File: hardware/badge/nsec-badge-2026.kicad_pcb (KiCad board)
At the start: 4 copper layers, 159.8 x 139.1 mm, 180 parts, among them J1001 Conn_01x01_Female, J1002 Conn_01x01_Female, J1003 Conn_01x01_Female, J1004 Conn_01x01_Female, J1005 Conn_01x01_Female, J1006 Conn_01x01_Female, J1007 Conn_01x01_Female, J1008 Conn_01x01_Female, J701 PM254-2-03-S-8_5, J702 PM254-2-03-S-8_5, J901 Bus_PCI_32bit_Universal, P1001 U.FL-R-SMT-1_10_, P1002 U.FL-R-SMT-1_10_, Q1201 IRLML0100TRPBF, SW201 TS-1187A-C-C-B, SW202 TS-1187A-C-C-B, SW601 TS-1187A-C-C-B, SW602 TS-1187A-C-C-B, SW603 TS-1187A-C-C-B, SW604 TS-1187A-C-C-B, SW605 TS-1187A-C-C-B, SW606 TS-1187A-C-C-B, U1001 ST25R3916-AQWT, U1101 VEML6040A3OG, U1202 HC-FPC-05-09-24RLTAG, U201 ESP32-S3-WROOM-1(N16R8), U301 AP2112K-3_3TRG1, U401 TYPE-C-31-M-12, U402 TPSMF05CT1G, U801 XT4054K421MR-G, U802 XDWF-0920-02P, Y1001 27.12Mhz

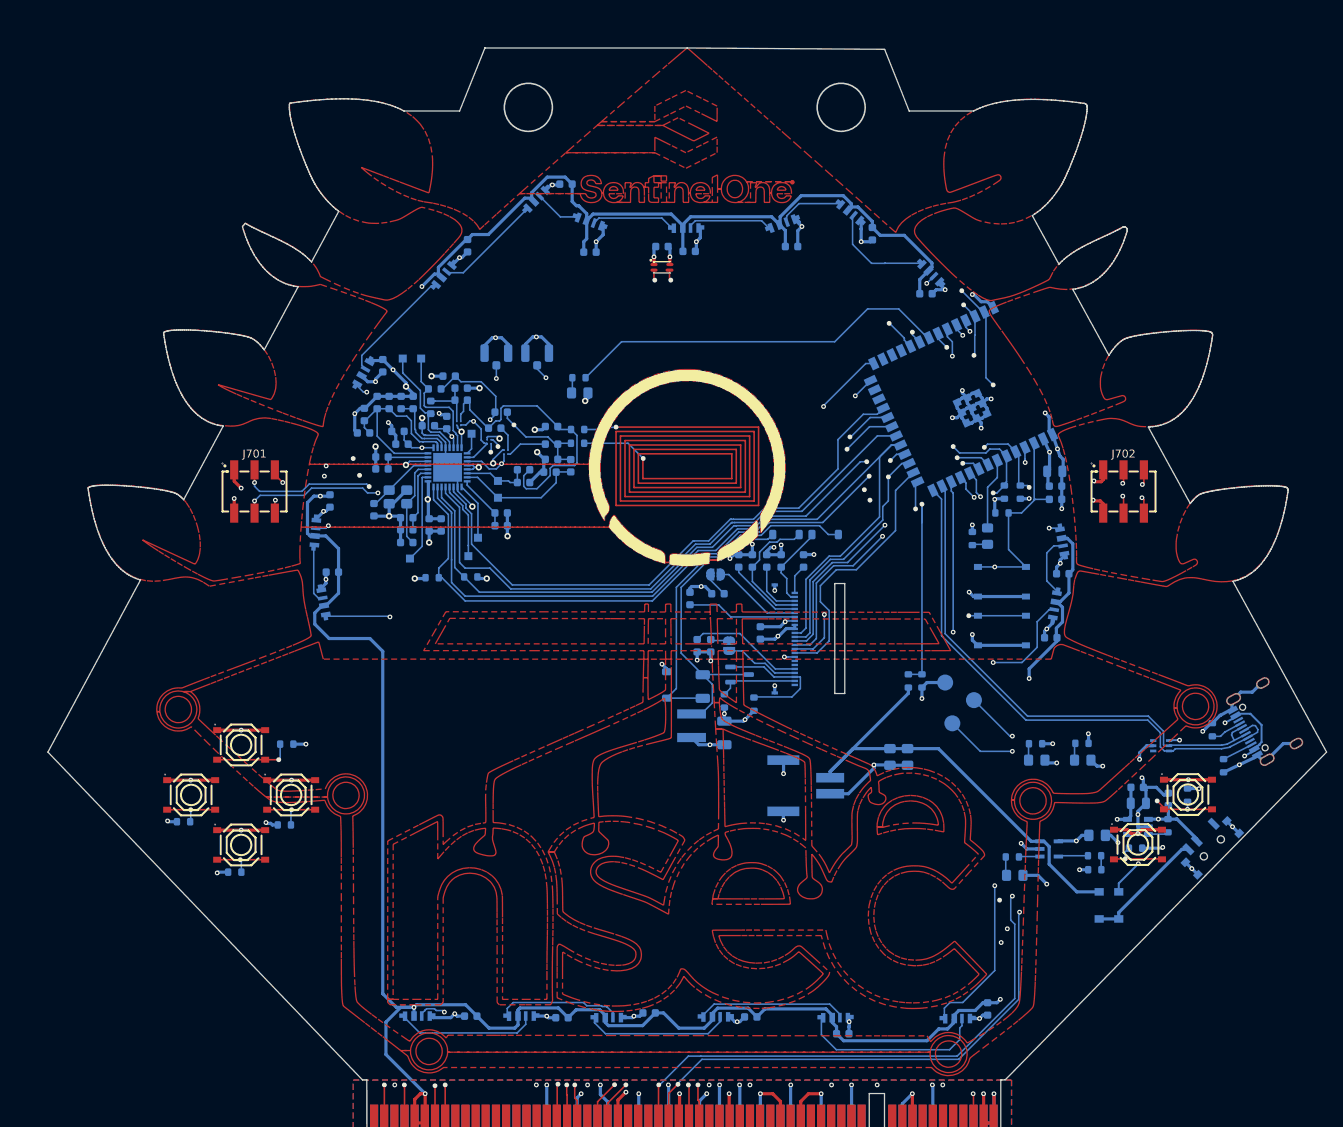
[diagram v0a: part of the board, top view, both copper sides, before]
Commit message: feat: badge v2 PCB design with panelization support
Updated schematic and PCB layout for badge v2 revision. Added
panelization project with JLCPCB production files, panelize script,
and board SVG artwork.
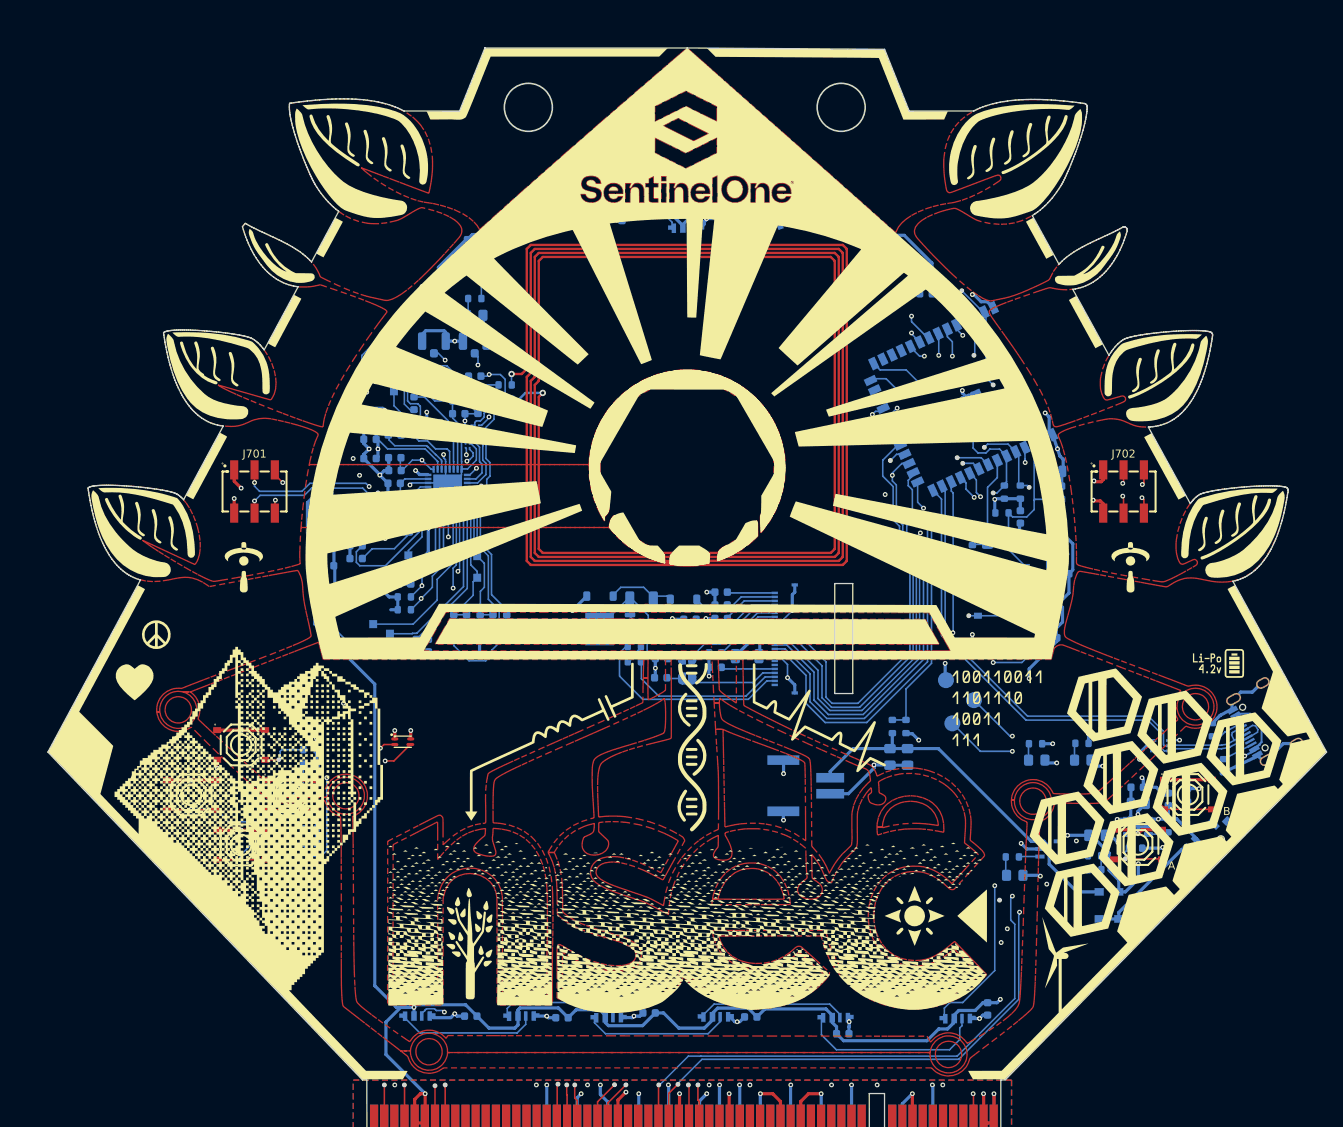
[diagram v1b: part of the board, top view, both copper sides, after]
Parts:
- removed the ? at (29.3, 30.1)
- added ? (x2): , Graphics, F.Cu at (29.4, 30.1)
- moved U1101 67.6 mm to (73.7, 116.8)
- moved C1101 56.1 mm to (150.9, 88.7), turned to -90 degrees
- moved C1030 27.9 mm to (84.1, 104.1)
- moved C1031 25.7 mm to (84.1, 105.9)
- moved C1035 24.3 mm to (80.1, 101.7), turned to -90 degrees
- moved C1029 22.8 mm to (86.7, 101.7), turned to -90 degrees
- moved C1034 21.3 mm to (81.7, 101.7), turned to 90 degrees
- moved D1203 19.5 mm to (108.8, 99.0), turned to 0 degrees
- moved C1032 19.3 mm to (85.0, 101.7), turned to 90 degrees
- moved C1006 18.9 mm to (76.9, 104.8), turned to -90 degrees
- moved C1004 18.3 mm to (75.4, 104.8), turned to -90 degrees
- moved D1201 18.2 mm to (108.8, 103.8)
- moved C1033 18.1 mm to (83.4, 101.7), turned to -90 degrees
- moved L1201 16.7 mm to (98.3, 102.7)
- moved R1001 16.4 mm to (82.7, 61.4)
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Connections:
- net Net-(R1004-Pad2) renamed /NFC/NFC_COIL
- C1011 pad 1: /NFC/VDD_TX -> +3V3
- C1012 pad 1: /NFC/VDD_TX -> +3V3
- C1015 pad 1: /NFC/VDD_TX -> +3V3
- C1016 pad 1: /NFC/VDD_TX -> +3V3
- C801 pad 1: VDD -> VBUS
- LED801 pad 2: VDD -> VBUS
- U1001 pad 10: /NFC/VDD_TX -> +3V3
- U1001 pad 8: /NFC/VDD_TX -> +3V3
- U801 pad 4: VDD -> VBUS
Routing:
- net /NFC/NFC_COIL: track 12.6 -> 616.7 mm
- net GND: track 395.7 -> 497.3 mm, vias 108 -> 103
- net /ESP32-S3/GPIO21: track 73.0 -> 123.2 mm, vias 0 -> 2
- net /ESP32-S3/GPIO12: track 74.0 -> 121.8 mm, vias 0 -> 2
- net Net-(C1026-Pt2): track 18.6 -> 65.0 mm, vias 2 -> 3
- net /SPI_MISO: track 79.7 -> 123.7 mm, vias 2 -> 3
- net Net-(D1202-A): track 42.8 -> 8.60 mm
- net +3V3: track 123.0 -> 152.5 mm, vias 29 -> 26
- net /ESP32-S3/GPIO45: track 38.8 -> 67.6 mm
- net /ESP32-S3/GPIO40: track 48.0 -> 75.1 mm, vias 0 -> 2
- net Net-(D1201-A): track 39.2 -> 12.3 mm
- net /NFC/VDD_TX: track 25.5 -> 0.00 mm
- net VBUS: track 40.9 -> 63.0 mm, vias 4 -> 6
- net /BTN_UP: track 172.1 -> 193.1 mm, vias 3 -> 4
- net Net-(C1027-Pt1): track 5.19 -> 25.8 mm
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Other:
- outline, holes or cut-outs redrawn
- board text added: "MCU provided by"
- board text added: "nsec badge 2026"
- board text removed: "nsec badge proto v1"
